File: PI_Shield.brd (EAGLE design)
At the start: 78.7 x 69.5 mm, 64 parts, among them Q1 220mA/50V/3.5Ω, Q3 220mA/50V/3.5Ω, Q4 220mA/50V/3.5Ω, Q5 2.5A/30V/105mΩ, U1 MAX1136EUA-T, U2 AZ1117EH-3.3TRG1, Y1 ECS-80-S-4X

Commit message: Update PI_Shield.brd
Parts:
- moved R20 1.27 mm to (85.1, 36.8)
- moved U$12 1.27 mm to (82.5, 50.8)
- moved U$9 1.27 mm to (82.5, 43.2)
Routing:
- net 5V: track 148.9 -> 152.5 mm
- net MISO: track 34.9 -> 36.1 mm
- net SCL: track 122.1 -> 123.2 mm
- net PWM: track 62.6 -> 63.6 mm
- net DI: track 76.3 -> 75.4 mm

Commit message: Update PI_Shield.brd
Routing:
- net 3V3: track 274.2 -> 272.9 mm
- net SDA: track 108.4 -> 107.5 mm
- net PWM: track 63.6 -> 63.1 mm
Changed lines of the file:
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@@
 <contactref element="C2" pad="2"/>
 <contactref element="Y1" pad="1"/>
-<wire x1="73.66" y1="57.25" x2="73.56" y2="57.15" width="0.3048" layer="1"/>
 <wire x1="73.66" y1="57.25" x2="79.345" y2="57.25" width="0.3048" layer="1"/>
 <wire x1="79.345" y1="57.25" x2="80.715" y2="55.88" width="0.3048" layer="1"/>
@@
 <wire x1="51.56" y1="57.15" x2="51.0948" y2="56.6848" width="0.3048" layer="1"/>
 <wire x1="51.0948" y1="56.6848" x2="45.72" y2="56.6848" width="0.3048" layer="1"/>
-<wire x1="45.72" y1="56.6848" x2="45.46375" y2="56.6848" width="0.3048" layer="1"/>
 <wire x1="33.02" y1="52.07" x2="34.29" y2="53.34" width="0.3048" layer="1"/>
 <wire x1="45.72" y1="56.6848" x2="41.44483125" y2="56.6848" width="0.254" layer="1"/>
@@
 <wire x1="31.85" y1="18.73" x2="31.75" y2="18.63" width="0.3048" layer="1"/>
 <wire x1="64.77" y1="47.84" x2="64.56" y2="48.05" width="0.3048" layer="1"/>
-<wire x1="64.56" y1="48.05" x2="64.35" y2="48.26" width="0.3048" layer="1"/>
-<wire x1="45.72" y1="55.46" x2="45.93" y2="55.67" width="0.3048" layer="1"/>
 <wire x1="45.93" y1="55.67" x2="46.14" y2="55.88" width="0.3048" layer="1"/>
 <wire x1="74.27285" y1="44.6188" x2="74.10405" y2="44.45" width="0.3048" layer="1"/>
@@
 <wire x1="45.72" y1="12.28" x2="47.41" y2="12.28" width="0.254" layer="16"/>
 <wire x1="47.41" y1="12.28" x2="48.26" y2="11.43" width="0.254" layer="16"/>
-<wire x1="48.26" y1="11.43" x2="49.53" y2="10.16" width="0.254" layer="16"/>
-<wire x1="49.53" y1="10.16" x2="49.657" y2="10.033" width="0.254" layer="16"/>
+<wire x1="48.26" y1="11.43" x2="49.657" y2="10.033" width="0.254" layer="16"/>
 <wire x1="65.913" y1="10.033" x2="67.31" y2="11.43" width="0.254" layer="16"/>
 <wire x1="49.657" y1="10.033" x2="65.913" y2="10.033" width="0.254" layer="16"/>
 <wire x1="50.8" y1="27.52" x2="54.61" y2="31.33" width="0.254" layer="1"/>
 <wire x1="54.61" y1="31.33" x2="58.42" y2="31.33" width="0.254" layer="1"/>
-<wire x1="58.84" y1="31.33" x2="58.42" y2="31.33" width="0.254" layer="1"/>
 <wire x1="30.75" y1="36.51" x2="31.75" y2="35.51" width="0.254" layer="1"/>
 <wire x1="31.75" y1="32.6" x2="30.9" y2="31.75" width="0.254" layer="1"/>
@@
 <wire x1="50.2" y1="51.22" x2="51.56" y2="52.58" width="0.254" layer="1"/>
 <wire x1="60.96" y1="26.67" x2="59.69" y2="26.67" width="0.254" layer="1"/>
-<wire x1="58.42" y1="31.07513125" x2="58.42" y2="31.33" width="0.254" layer="1"/>
 <wire x1="59.69" y1="26.67" x2="59.1994" y2="27.1606" width="0.254" layer="1"/>
 <wire x1="59.1994" y1="30.29573125" x2="59.1994" y2="27.1606" width="0.254" layer="1"/>
-<wire x1="58.42" y1="31.33" x2="59.27" y2="31.33" width="0.254" layer="1"/>
 <wire x1="59.69" y1="30.78633125" x2="59.1994" y2="30.29573125" width="0.254" layer="1"/>
-<wire x1="59.27" y1="31.33" x2="59.69" y2="30.91" width="0.254" layer="1"/>
+<wire x1="59.69" y1="30.91" x2="59.27" y2="31.33" width="0.254" layer="1"/>
 <wire x1="59.69" y1="30.91" x2="59.69" y2="30.78633125" width="0.254" layer="1"/>
 <wire x1="43.18" y1="27.52" x2="42.76" y2="27.94" width="0.254" layer="1"/>
@@
 <wire x1="44.45" y1="54.61" x2="45.51" y2="55.67" width="0.254" layer="1"/>
 <wire x1="45.51" y1="55.67" x2="45.93" y2="55.67" width="0.254" layer="1"/>
-<wire x1="48.26" y1="11.43" x2="48.26" y2="11.43" width="0.254" layer="16"/>
+<wire x1="59.27" y1="31.33" x2="58.42" y2="31.33" width="0.254" layer="1"/>
 </signal>
 <signal name="N$1">
@@
 <contactref element="R6" pad="1"/>
 <contactref element="R7" pad="2"/>
-<wire x1="66.46" y1="22.86" x2="66.46" y2="22.43" width="0.3048" layer="1"/>
 <wire x1="66.46" y1="22.86" x2="64.77" y2="24.55" width="0.3048" layer="1"/>
 <wire x1="64.77" y1="24.55" x2="64.77" y2="25.82" width="0.3048" layer="1"/>
-<wire x1="66.46" y1="22.86" x2="66.46" y2="22.01" width="0.254" layer="1"/>
-<wire x1="66.46" y1="22.01" x2="66.04" y2="21.59" width="0.254" layer="1"/>
-<wire x1="66.04" y1="21.59" x2="64.77" y2="21.59" width="0.254" layer="1"/>
+<wire x1="64.77" y1="21.59" x2="66.04" y2="21.59" width="0.254" layer="1"/>
 <wire x1="64.77" y1="21.59" x2="64.35" y2="21.17" width="0.254" layer="1"/>
 <wire x1="64.35" y1="21.17" x2="64.35" y2="20.32" width="0.254" layer="1"/>
+<wire x1="66.04" y1="21.59" x2="66.46" y2="22.01" width="0.254" layer="1"/>
+<wire x1="66.46" y1="22.01" x2="66.46" y2="22.86" width="0.254" layer="1"/>
 </signal>
 <signal name="DI1">
@@
 <contactref element="Q3" pad="2"/>
 <contactref element="R12" pad="1"/>
-<wire x1="53.34" y1="15.24" x2="53.34" y2="16.51" width="0.3048" layer="1"/>
 <wire x1="53.34" y1="16.51" x2="53.34" y2="13.55" width="0.3048" layer="1"/>
 <wire x1="53.34" y1="13.55" x2="52.07" y2="12.28" width="0.3048" layer="1"/>
@@
 <wire x1="20.6148" y1="18.7198" x2="17.78" y2="15.885" width="0.3048" layer="1"/>
 <wire x1="25.4100875" y1="18.7198" x2="20.6148" y2="18.7198" width="0.3048" layer="1"/>
-<wire x1="17.78" y1="36.205" x2="15.24" y2="33.665" width="0.3048" layer="1"/>
 <wire x1="15.24" y1="33.665" x2="15.24" y2="26.67" width="0.3048" layer="1"/>
 <wire x1="15.24" y1="26.67" x2="15.865" y2="26.045" width="0.3048" layer="1"/>
@@
 <wire x1="54.61" y1="15.24" x2="53.34" y2="16.51" width="0.254" layer="16"/>
 <wire x1="80.01" y1="15.24" x2="54.61" y2="15.24" width="0.254" layer="16"/>
+<wire x1="17.78" y1="36.205" x2="17.135" y2="35.56" width="0.254" layer="1"/>
+<wire x1="17.135" y1="35.56" x2="16.51" y2="35.56" width="0.254" layer="1"/>
+<wire x1="16.51" y1="35.56" x2="15.24" y2="34.29" width="0.254" layer="1"/>
+<wire x1="15.24" y1="34.29" x2="15.24" y2="33.665" width="0.254" layer="1"/>
 </signal>
 <signal name="SCL">
@@
 <wire x1="87.63" y1="48.26" x2="85.085" y2="50.805" width="0.3048" layer="16"/>
 <wire x1="85.085" y1="50.805" x2="83.8" y2="50.805" width="0.3048" layer="16"/>
-<wire x1="81.0012" y1="34.5688" x2="81.28" y2="34.29" width="0.3048" layer="1"/>
 <wire x1="60.6812" y1="34.5688" x2="60.96" y2="34.5688" width="0.3048" layer="1"/>
 <wire x1="36.83" y1="23.71" x2="31.75" y2="23.71" width="0.762" layer="1"/>
@@
 <wire x1="38.52" y1="27.09" x2="38.52" y2="30.48" width="0.762" layer="1"/>
 <wire x1="36.83" y1="25.4" x2="38.52" y2="27.09" width="0.762" layer="1"/>
-<wire x1="35.2044" y1="28.9306" x2="36.7538" y2="30.48" width="0.762" layer="1"/>
-<wire x1="36.7538" y1="30.48" x2="38.52" y2="30.48" width="0.762" layer="1"/>
 <wire x1="38.52" y1="30.48" x2="38.31" y2="30.69" width="0.762" layer="1"/>
 <wire x1="38.31" y1="30.69" x2="38.31" y2="37.89" width="0.762" layer="1"/>
@@
 <wire x1="80.01" y1="36.83" x2="81.28" y2="35.56" width="0.254" layer="16"/>
 <wire x1="87.63" y1="39.37" x2="81.28" y2="39.37" width="0.254" layer="16"/>
+<wire x1="35.2044" y1="28.9306" x2="36.7538" y2="30.48" width="0.6096" layer="1"/>
+<wire x1="36.7538" y1="30.48" x2="38.52" y2="30.48" width="0.6096" layer="1"/>
 </signal>
 <signal name="IMU_INT">
@@
 <contactref element="R20" pad="1"/>
 <contactref element="PCB1" pad="P$31"/>
-<wire x1="85.09" y1="35.98" x2="84.67" y2="35.98" width="0.3048" layer="1"/>
 <wire x1="82.55" y1="43.175" x2="82.55" y2="38.1" width="0.3048" layer="1"/>
 <wire x1="27.5082" y1="55.3466" x2="29.9974" y2="52.8574" width="0.3048" layer="16"/>
@@
 <wire x1="76.28046875" y1="50.795" x2="77.13426875" y2="49.9412" width="0.3048" layer="16"/>
 <wire x1="27.5082" y1="57.8866" x2="29.21" y2="57.8866" width="0.3048" layer="16"/>
-<wire x1="29.21" y1="57.8866" x2="29.7434" y2="57.8866" width="0.3048" layer="16"/>
-<wire x1="29.21" y1="57.8866" x2="32.0323875" y2="57.8866" width="0.254" layer="16"/>
 <wire x1="32.0323875" y1="57.8866" x2="32.5657875" y2="58.42" width="0.254" layer="16"/>
 <wire x1="43.18" y1="49.53" x2="59.695" y2="49.53" width="0.254" layer="16"/>
@@
 <wire x1="82.55" y1="49.53" x2="82.55" y2="50.795" width="0.254" layer="16"/>
 <wire x1="78.74" y1="48.26" x2="81.28" y2="48.26" width="0.254" layer="16"/>
+<wire x1="29.21" y1="57.8866" x2="32.0323875" y2="57.8866" width="0.254" layer="16"/>
 </signal>
 <signal name="TX">
@@
 <wire x1="30.8356" y1="28.9306" x2="32.385" y2="30.48" width="0.3048" layer="1"/>
 <wire x1="32.385" y1="30.48" x2="34.29" y2="30.48" width="0.3048" layer="1"/>
-<wire x1="32.85" y1="35.56" x2="33.02" y2="35.56" width="0.254" layer="1"/>
+<wire x1="35.98" y1="35.56" x2="36.83" y2="34.71" width="0.254" layer="1"/>
 <wire x1="32.85" y1="35.56" x2="35.98" y2="35.56" width="0.254" layer="1"/>
-<wire x1="35.98" y1="35.56" x2="36.83" y2="34.71" width="0.254" layer="1"/>
 </signal>
 <signal name="SDA_ADC">

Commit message: Update PI_Shield.brd
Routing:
- net SCL: track 123.2 -> 127.5 mm, vias 0 -> 4
- net CS: track 29.0 -> 32.7 mm
- net PI_POWER: track 0.00 -> 2.54 mm
- net SDA_ADC: track 19.8 -> 20.7 mm
- net INT: track 23.5 -> 24.3 mm
- net 5V: track 152.1 -> 152.9 mm
- net CLK: track 33.1 -> 33.8 mm
- net RESET: track 11.4 -> 11.9 mm
- added copper zone on layer 16, net GND

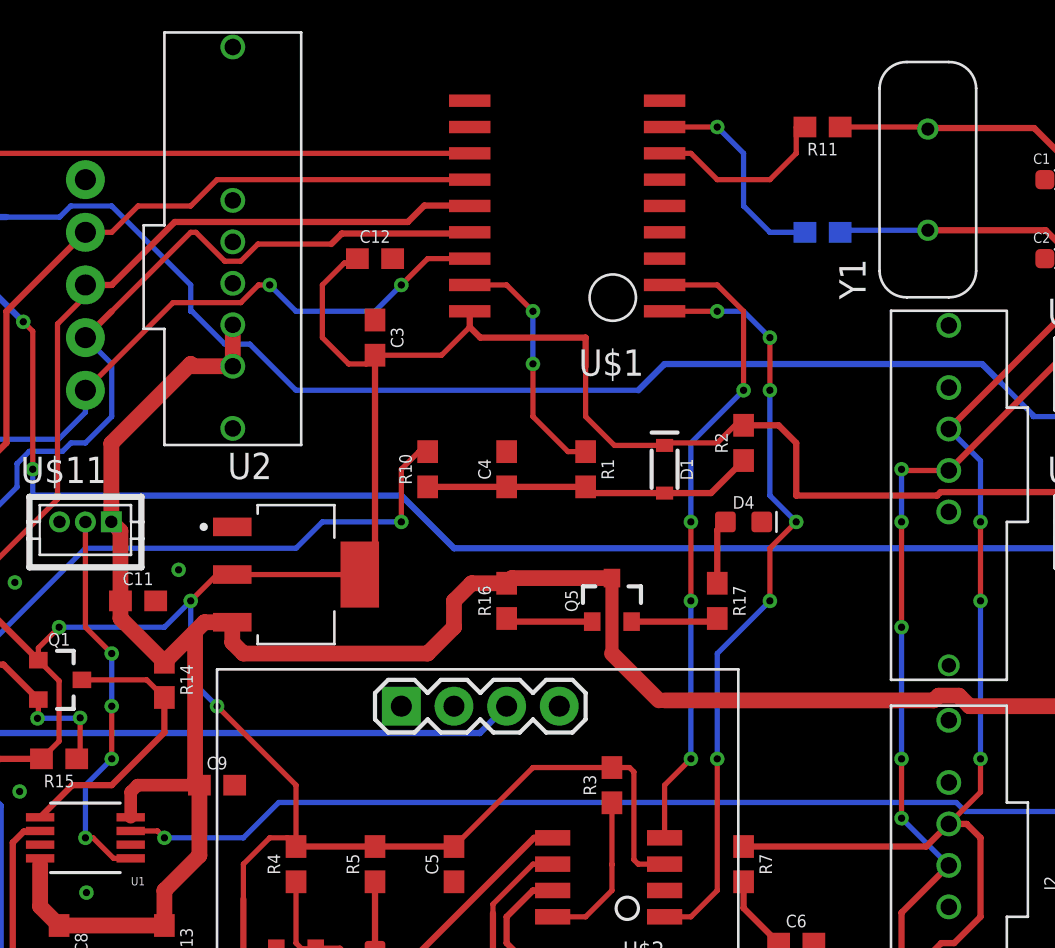
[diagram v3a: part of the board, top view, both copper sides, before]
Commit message: Length of wires updated
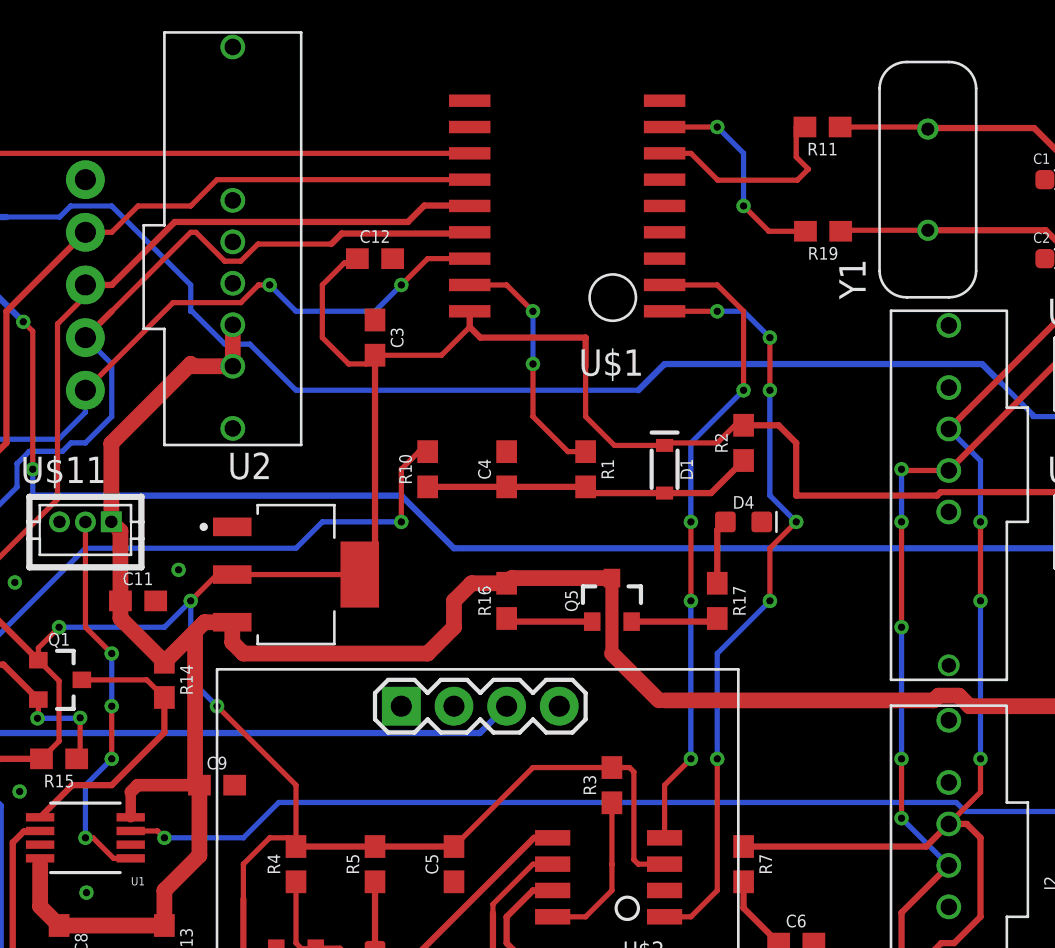
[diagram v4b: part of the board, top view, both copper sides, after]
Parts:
- moved R19 0.06 mm to (68.6, 57.2), flipped to the top, turned to 180 degrees
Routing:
- net OSC2: track 9.09 -> 10.4 mm
- net OSC1: vias 1 -> 2
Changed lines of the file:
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@@
 <attribute name="VALUE" x="68.58" y="62.992" size="0.6096" layer="27" font="vector" ratio="20" rot="R180" align="top-center"/>
 </element>
-<element name="R19" library="SparkFun-Resistors" library_urn="urn:adsk.eagle:library:532" package="0603" package3d_urn="urn:adsk.eagle:package:39650/1" value="0" x="68.58" y="57.15" smashed="yes" rot="MR0">
-<attribute name="NAME" x="68.58" y="57.912" size="0.6096" layer="26" font="vector" ratio="20" rot="MR0" align="bottom-center"/>
-<attribute name="PROD_ID" value=" " x="68.58" y="57.15" size="1.778" layer="28" rot="MR0" display="off"/>
-<attribute name="VALUE" x="68.58" y="56.388" size="0.6096" layer="28" font="vector" ratio="20" rot="MR0" align="top-center"/>
+<element name="R19" library="SparkFun-Resistors" library_urn="urn:adsk.eagle:library:532" package="0603" package3d_urn="urn:adsk.eagle:package:39650/1" value="0" x="68.6054" y="57.2008" smashed="yes" rot="R180">
+<attribute name="NAME" x="68.6054" y="56.4388" size="0.6096" layer="25" font="vector" ratio="20" rot="R180" align="bottom-center"/>
+<attribute name="PROD_ID" value=" " x="68.6054" y="57.2008" size="1.778" layer="27" rot="R180" display="off"/>
+<attribute name="VALUE" x="68.6054" y="57.9628" size="0.6096" layer="27" font="vector" ratio="20" rot="R180" align="top-center"/>
 </element>
 </elements>
@@
 <wire x1="79.345" y1="57.25" x2="80.715" y2="55.88" width="0.3048" layer="1"/>
 <contactref element="R19" pad="1"/>
-<wire x1="69.43" y1="57.15" x2="69.53" y2="57.25" width="0.254" layer="16"/>
-<wire x1="69.53" y1="57.25" x2="73.66" y2="57.25" width="0.254" layer="16"/>
+<wire x1="69.4554" y1="57.2008" x2="69.5046" y2="57.25" width="0.254" layer="1"/>
+<wire x1="69.5046" y1="57.25" x2="73.66" y2="57.25" width="0.254" layer="1"/>
 </signal>
 <signal name="GND">
@@
 <contactref element="U$1" pad="OSC1"/>
 <contactref element="R19" pad="2"/>
-<wire x1="67.73" y1="57.15" x2="66.04" y2="57.15" width="0.254" layer="16"/>
-<wire x1="66.04" y1="57.15" x2="64.77" y2="58.42" width="0.254" layer="16"/>
-<wire x1="64.77" y1="58.42" x2="64.77" y2="60.96" width="0.254" layer="16"/>
+<wire x1="64.77" y1="60.96" x2="64.77" y2="58.42" width="0.254" layer="16"/>
 <wire x1="64.77" y1="60.96" x2="63.5" y2="62.23" width="0.254" layer="16"/>
 <via x="63.5" y="62.23" extent="1-16" drill="0.35"/>
 <wire x1="63.5" y1="62.23" x2="60.96" y2="62.23" width="0.254" layer="1"/>
+<via x="64.77" y="58.42" extent="1-16" drill="0.35"/>
+<wire x1="64.77" y1="58.42" x2="65.9892" y2="57.2008" width="0.254" layer="1"/>
+<wire x1="65.9892" y1="57.2008" x2="67.7554" y2="57.2008" width="0.254" layer="1"/>
 </signal>
 <signal name="OSC2">
@@
 <wire x1="67.73" y1="62.23" x2="67.31" y2="62.23" width="0.254" layer="1"/>
 <wire x1="60.96" y1="60.96" x2="62.23" y2="60.96" width="0.254" layer="1"/>
-<wire x1="62.23" y1="60.96" x2="63.5" y2="59.69" width="0.254" layer="1"/>
-<wire x1="63.5" y1="59.69" x2="66.04" y2="59.69" width="0.254" layer="1"/>
-<wire x1="66.04" y1="59.69" x2="67.31" y2="60.96" width="0.254" layer="1"/>
-<wire x1="67.31" y1="60.96" x2="67.31" y2="62.23" width="0.254" layer="1"/>
+<wire x1="62.23" y1="60.96" x2="63.5254" y2="59.6646" width="0.254" layer="1"/>
+<wire x1="67.31" y1="60.7822" x2="67.31" y2="62.23" width="0.254" layer="1"/>
+<wire x1="67.8942" y1="60.198" x2="67.31" y2="60.7822" width="0.254" layer="1"/>
+<wire x1="67.3608" y1="59.6646" x2="67.8942" y2="60.198" width="0.254" layer="1"/>
+<wire x1="63.5254" y1="59.6646" x2="67.3608" y2="59.6646" width="0.254" layer="1"/>
 </signal>
 <signal name="TXCAN">
@@
 <wire x1="87.63" y1="39.37" x2="81.28" y2="39.37" width="0.254" layer="16"/>
 <wire x1="35.5346" y1="30.48" x2="35.2044" y2="30.1498" width="0.6096" layer="1"/>
-<wire x1="35.2044" y1="28.9306" x2="35.2044" y2="30.1498" width="0.6096" layer="1"/>
+<wire x1="35.2044" y1="28.9306" x2="35.2044" y2="30.1498" width="0.508" layer="1"/>
 <wire x1="35.5346" y1="30.48" x2="38.52" y2="30.48" width="0.6096" layer="1"/>
 </signal>
